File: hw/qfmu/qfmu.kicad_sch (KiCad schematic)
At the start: 0 parts

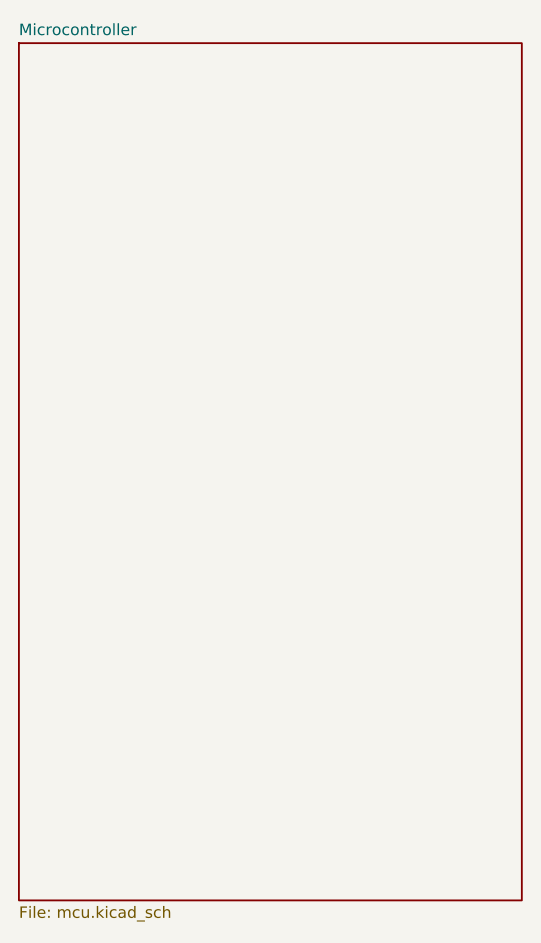
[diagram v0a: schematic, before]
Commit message: feat: add material list and create library dir
Create a spreadsheet to annotate BOM and include symbols in lib/
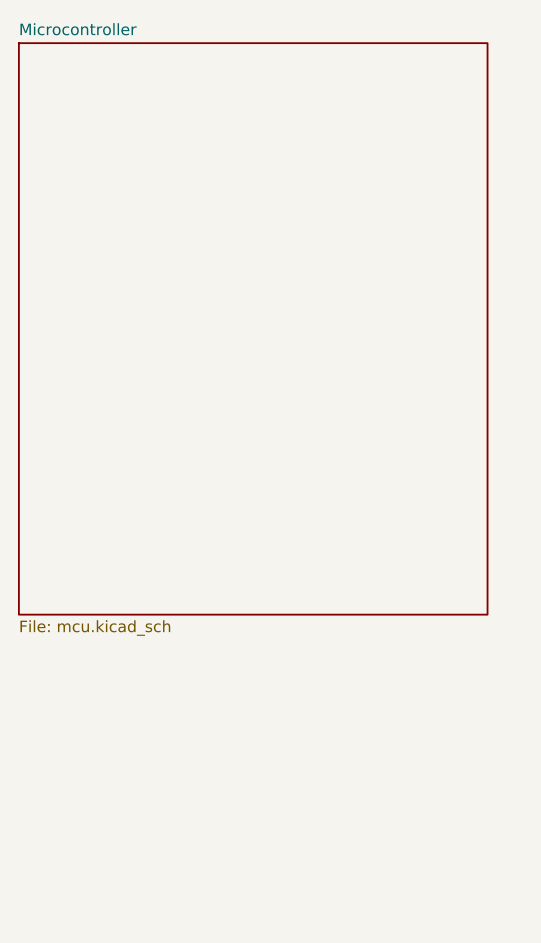
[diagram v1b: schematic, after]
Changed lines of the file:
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@@
 	(sheet
 		(at 110.49 53.34)
-		(size 55.88 95.25)
+		(size 52.07 63.5)
 		(fields_autoplaced yes)
 		(stroke
@@
 		)
 		(property "Sheetfile" "mcu.kicad_sch"
-			(at 110.49 149.2 0)
+			(at 110.49 117.45 0)
 			(effects
 				(font

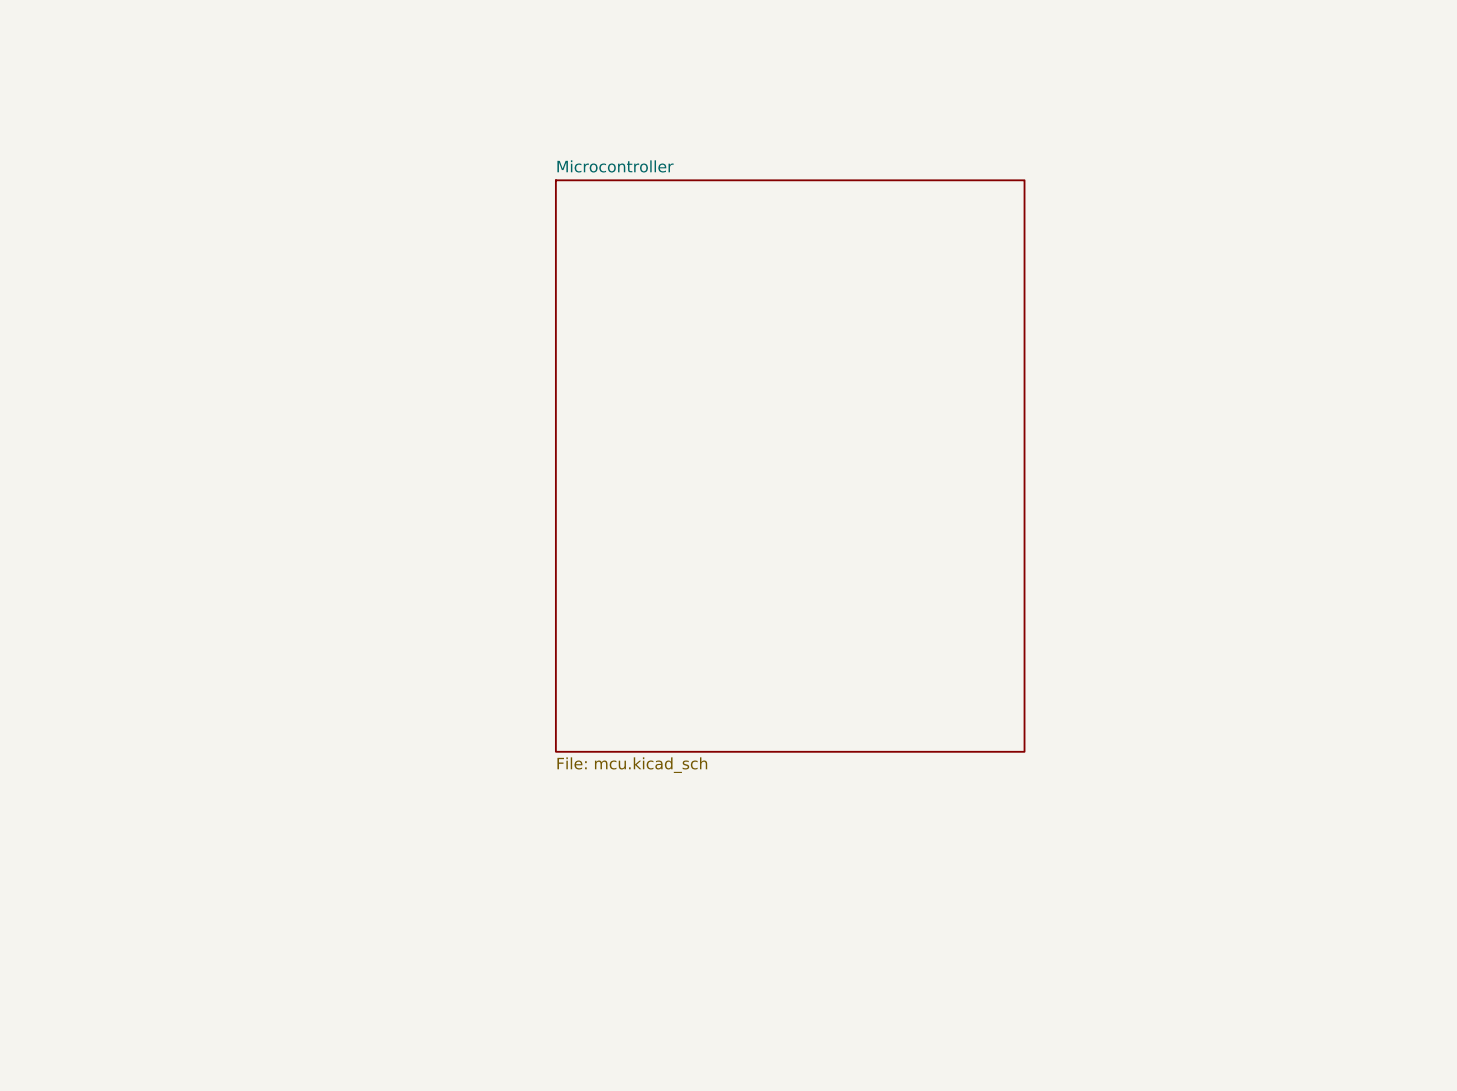
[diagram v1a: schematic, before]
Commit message: feat: add MCU, basic motor structure, sensors and power
Initialize basic structure for the motor, sensor and power sheets.
Update material list (mats.ods) with more components to be used.
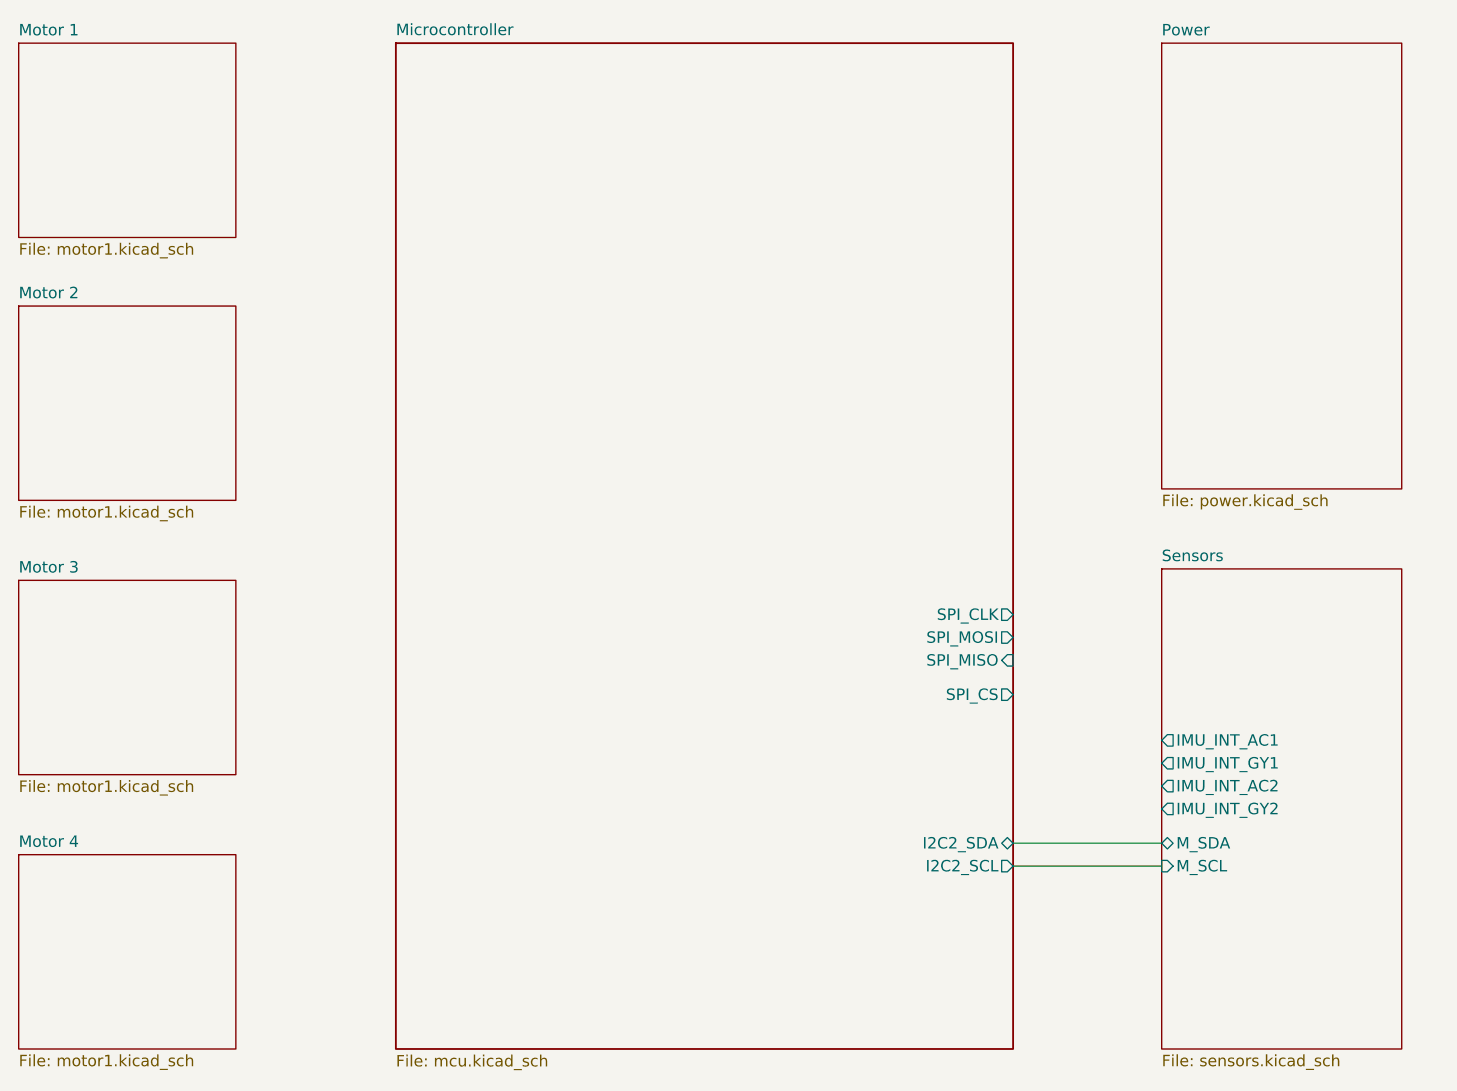
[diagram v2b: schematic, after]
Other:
- added sheet Motor 1 (motor1.kicad_sch)
- added sheet Motor 2 (motor1.kicad_sch)
- added sheet Motor 3 (motor1.kicad_sch)
- added sheet Motor 4 (motor1.kicad_sch)
- added sheet Power (power.kicad_sch)
- added sheet Sensors (sensors.kicad_sch)
- sheet Microcontroller ports: added I2C2_SCL, I2C2_SDA, SPI_CLK, SPI_CS, SPI_MISO, SPI_MOSI; removed none

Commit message: feat: add new BLDC controler and RF section
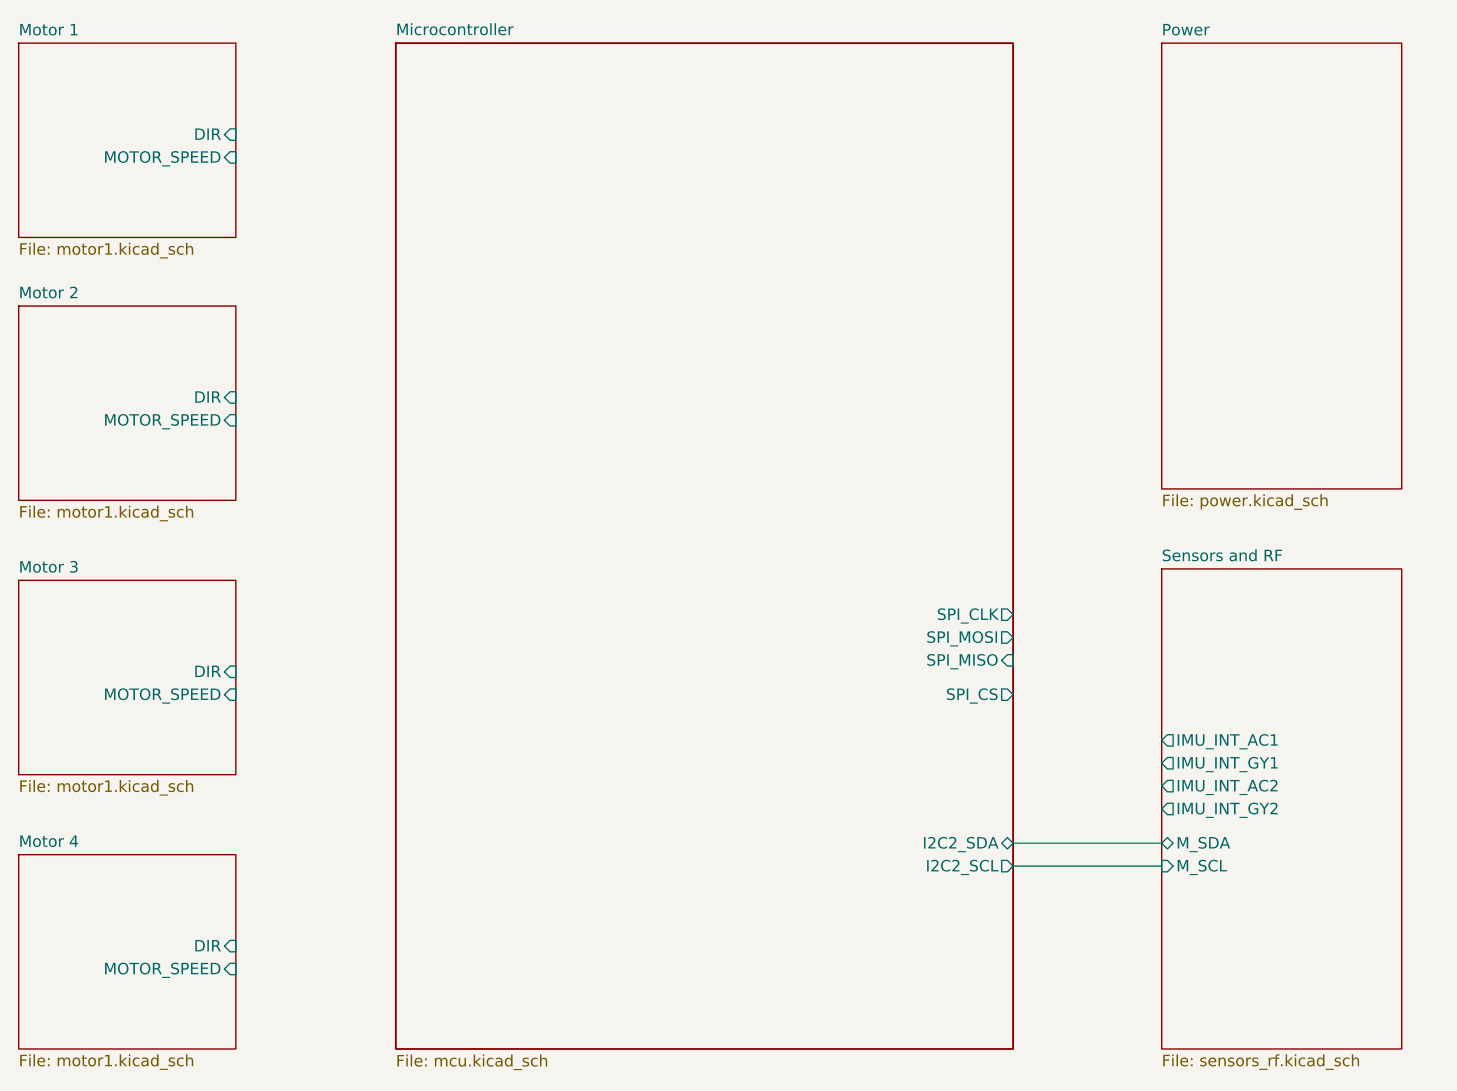
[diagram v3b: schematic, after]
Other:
- sheet Sensors renamed Sensors and RF
- sheet Motor 1 ports: added DIR, MOTOR_SPEED; removed none
- sheet Motor 2 ports: added DIR, MOTOR_SPEED; removed none
- sheet Motor 3 ports: added DIR, MOTOR_SPEED; removed none
- sheet Motor 4 ports: added DIR, MOTOR_SPEED; removed none
- sheet Sensors and RF: file sensors.kicad_sch -> sensors_rf.kicad_sch
- company: Daniel Pérez -> Daniel Enrique Pérez Díaz
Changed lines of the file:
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@@
 	(title_block
 		(title "Quincy FMU")
-		(date "2024-09-10")
+		(date "2024-09-28")
 		(rev "0")
-		(company "Daniel Pérez")
+		(company "Daniel Enrique Pérez Díaz")
 		(comment 1 "Flight Management Unit for the Quincy Quadcopter project.")
+		(comment 2 "Top Level Sheet")
 	)
 	(wire
@@
 			)
 		)
+		(pin "DIR" input
+			(at 74.93 77.47 0)
+			(effects
+				(font
+					(size 1.27 1.27)
+				)
+				(justify right)
+			)
+		)
+		(pin "MOTOR_SPEED" input
+			(at 74.93 80.01 0)
+			(effects
+				(font
+					(size 1.27 1.27)
+				)
+				(justify right)
+			)
+		)
 		(instances
 			(project "qfmu"
@@
 			)
 		)
+		(pin "DIR" input
+			(at 74.93 138.43 0)
+			(effects
+				(font
+					(size 1.27 1.27)
+				)
+				(justify right)
+			)
+		)
+		(pin "MOTOR_SPEED" input
+			(at 74.93 140.97 0)
+			(effects
+				(font
+					(size 1.27 1.27)
+				)
+				(justify right)
+			)
+		)
 		(instances
 			(project "qfmu"
@@
 			(color 0 0 0 0.0000)
 		)
-		(property "Sheetname" "Sensors"
+		(property "Sheetname" "Sensors and RF"
 			(at 177.8 95.8084 0)
 			(effects
@@
 			)
 		)
-		(property "Sheetfile" "sensors.kicad_sch"
+		(property "Sheetfile" "sensors_rf.kicad_sch"
 			(at 177.8 150.4446 0)
 			(effects
@@
 			)
 		)
+		(pin "DIR" input
+			(at 74.93 48.26 0)
+			(effects
+				(font
+					(size 1.27 1.27)
+				)
+				(justify right)
+			)
+		)
+		(pin "MOTOR_SPEED" input
+			(at 74.93 50.8 0)
+			(effects
+				(font
+					(size 1.27 1.27)
+				)
+				(justify right)
+			)
+		)
 		(instances
 			(project "qfmu"
@@
 			)
 		)
+		(pin "DIR" input
+			(at 74.93 107.95 0)
+			(effects
+				(font
+					(size 1.27 1.27)
+				)
+				(justify right)
+			)
+		)
+		(pin "MOTOR_SPEED" input
+			(at 74.93 110.49 0)
+			(effects
+				(font
+					(size 1.27 1.27)
+				)
+				(justify right)
+			)
+		)

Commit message: feat: finish motors, RF and power monitor
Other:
- sheet Microcontroller ports: added ANT_MODE, DCHG, DDSG, IMU_INT_AC1, IMU_INT_GY1, MON_ALERT, MON_RST_SHUT, MON_SCL, MON_SDA, RF_DEMOD, TX_ASK; removed none
- sheet Motor 1 ports: added CONT_FW_RX0, CONT_FW_TX0, DUTYFREQ; removed none
- sheet Motor 2 ports: added CONT_FW_RX0, CONT_FW_TX0, DUTYFREQ; removed none
- sheet Motor 3 ports: added CONT_FW_RX0, CONT_FW_TX0, DUTYFREQ; removed none
- sheet Motor 4 ports: added CONT_FW_RX0, CONT_FW_TX0, DUTYFREQ; removed none
- sheet Power ports: added DCHG, DDSG, MON_ALERT, MON_RST_SHUT, MON_SCL, MON_SDA; removed none
- sheet Sensors and RF ports: added ANT_MODE, RF_DEMOD, TX_ASK; removed IMU_INT_AC2, IMU_INT_GY2

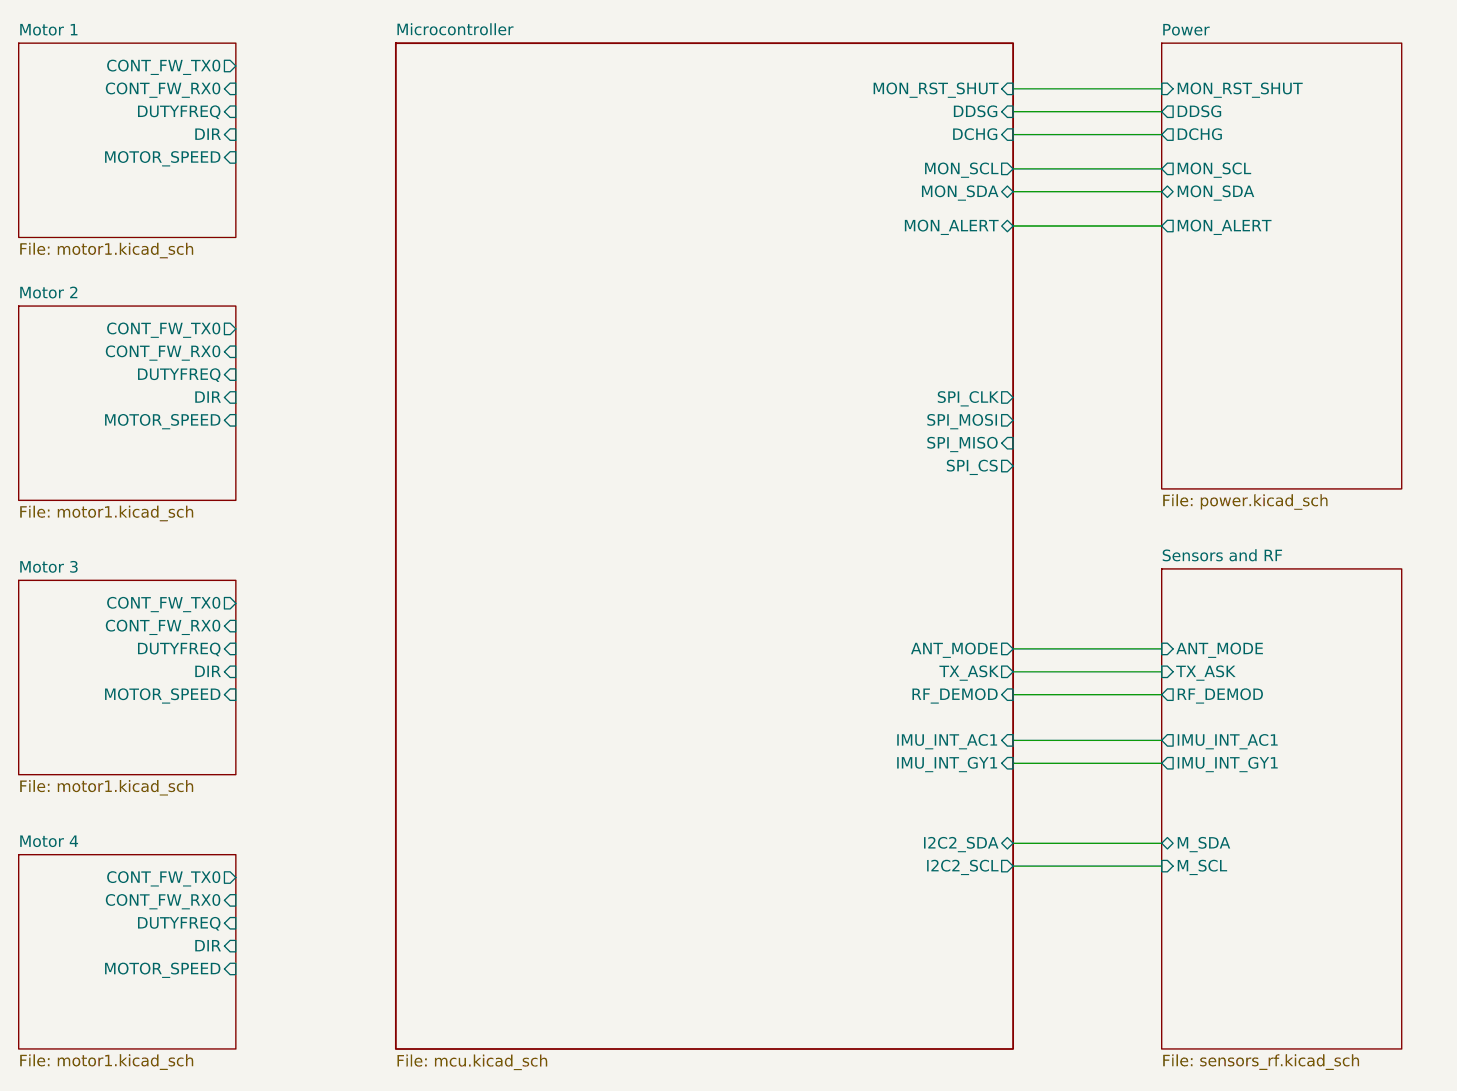
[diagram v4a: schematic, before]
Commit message: feat: start PCB design, define board outline and basic placement
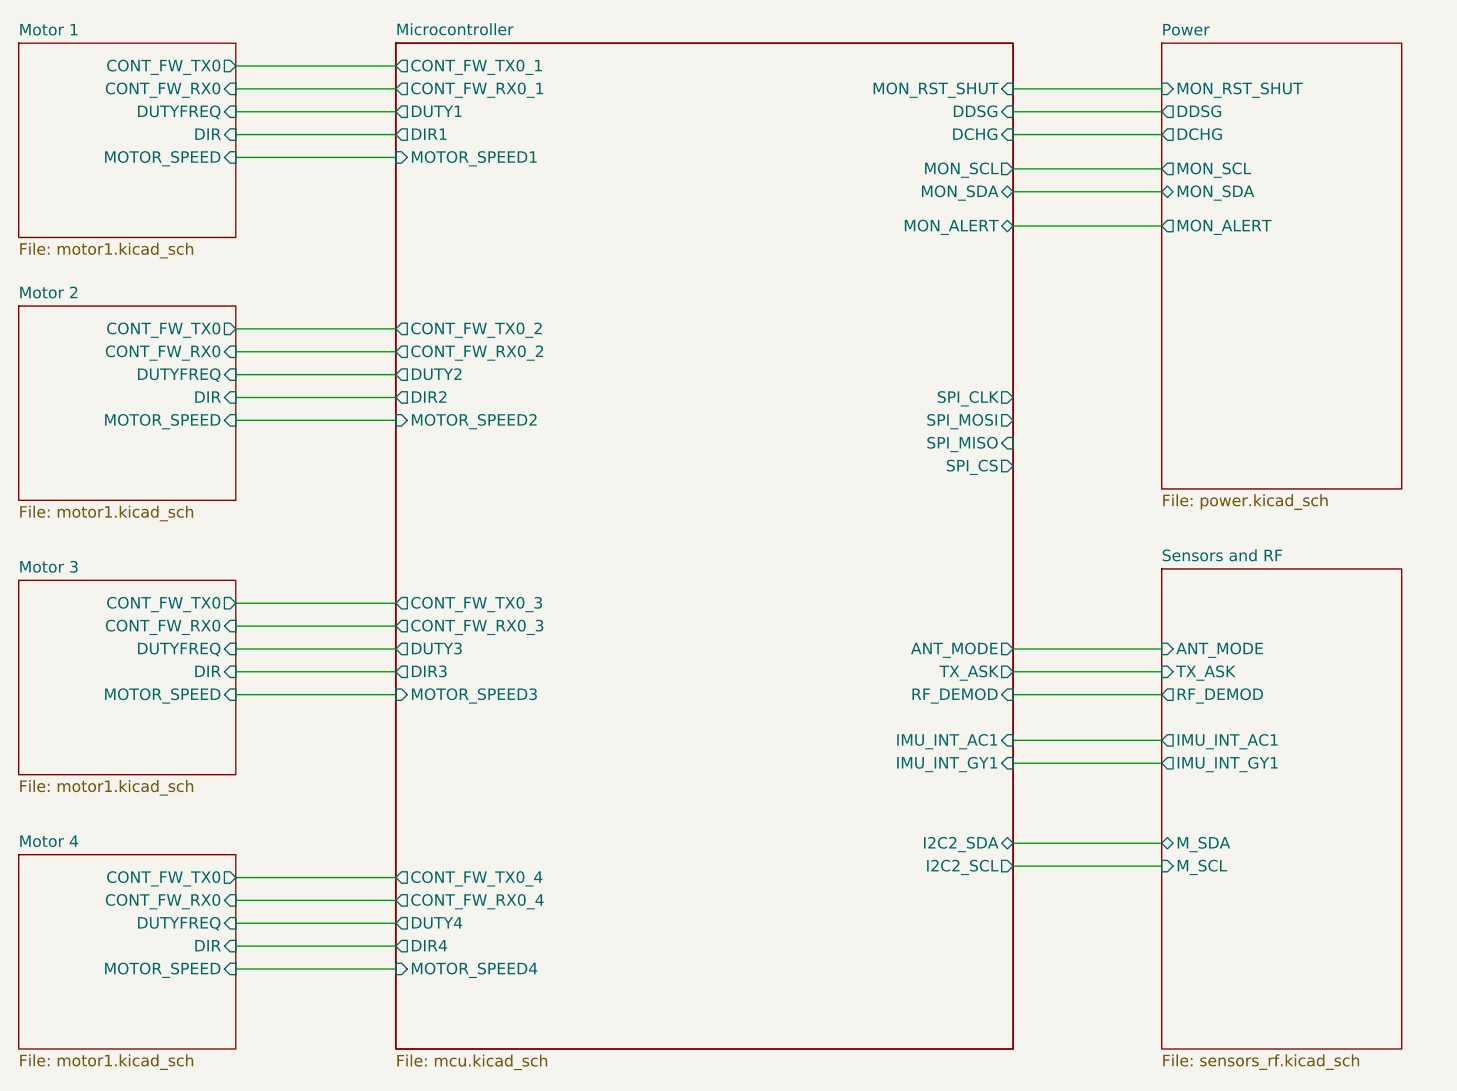
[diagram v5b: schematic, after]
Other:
- sheet Microcontroller ports: added CONT_FW_RX0_1, CONT_FW_RX0_2, CONT_FW_RX0_3, CONT_FW_RX0_4, CONT_FW_TX0_1, CONT_FW_TX0_2, CONT_FW_TX0_3, CONT_FW_TX0_4, DIR1, DIR2, DIR3, DIR4, DUTY1, DUTY2, DUTY3, DUTY4, MOTOR_SPEED1, MOTOR_SPEED2, MOTOR_SPEED3, MOTOR_SPEED4; removed none
